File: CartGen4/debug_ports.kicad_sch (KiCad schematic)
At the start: 2 parts, among them J2 Conn_01x05_Male, J3 Conn_02x09_Odd_Even

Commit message: Switched from 1.00mm to 1.27mm pin headers
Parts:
- J2: footprint Connector_PinHeader_1.00mm:PinHeader_1x05_P1.00mm_Vertical -> Connector_PinHeader_1.27mm:PinHeader_1x05_P1.27mm_Vertical
- J3: footprint Connector_PinHeader_1.00mm:PinHeader_2x09_P1.00mm_Vertical -> Connector_PinHeader_1.27mm:PinHeader_2x09_P1.27mm_Vertical
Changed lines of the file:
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@@
     (property "Reference" "J2" (id 0) (at 69.215 85.09 0))
     (property "Value" "Conn_01x05_Male" (id 1) (at 69.215 87.63 0))
-    (property "Footprint" "Connector_PinHeader_1.00mm:PinHeader_1x05_P1.00mm_Vertical" (id 2) (at 68.58 95.25 0)
+    (property "Footprint" "Connector_PinHeader_1.27mm:PinHeader_1x05_P1.27mm_Vertical" (id 2) (at 68.58 95.25 0)
       (effects (font (size 1.27 1.27)) hide)
     )
@@
     (property "Reference" "J3" (id 0) (at 196.85 81.28 0))
     (property "Value" "Conn_02x09_Odd_Even" (id 1) (at 196.85 83.82 0))
-    (property "Footprint" "Connector_PinHeader_1.00mm:PinHeader_2x09_P1.00mm_Vertical" (id 2) (at 195.58 97.79 0)
+    (property "Footprint" "Connector_PinHeader_1.27mm:PinHeader_2x09_P1.27mm_Vertical" (id 2) (at 195.58 97.79 0)
       (effects (font (size 1.27 1.27)) hide)
     )

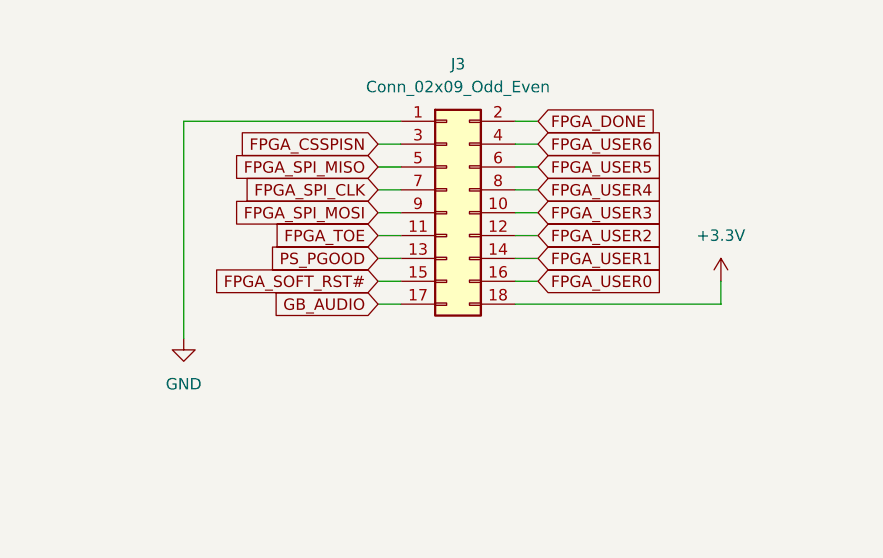
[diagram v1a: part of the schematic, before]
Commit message: Changed J3 to SMD header
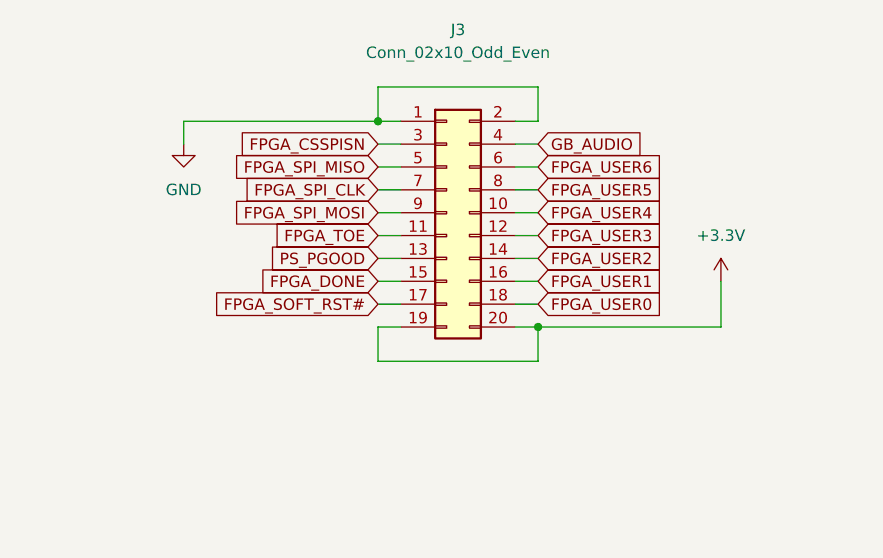
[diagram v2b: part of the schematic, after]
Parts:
- removed J3: Conn_02x09_Odd_Even, Connector_PinHeader_1.27mm:PinHeader_2x09_P1.27mm_Vertical, symbol Connector_Generic:Conn_02x09_Odd_Even
- added J3: Conn_02x10_Odd_Even, Connector:Conn_02x10, symbol Connector_Generic:Conn_02x10_Odd_Even
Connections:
- net +3V3: now also J3.19 (Pin_19), J3.20 (Pin_20)
- net FPGA_CSSPISN: now also J3.3 (Pin_3)
- net FPGA_DONE: now also J3.15 (Pin_15)
- net FPGA_SOFT_RST#: now also J3.17 (Pin_17)
- net FPGA_SPI_CLK: now also J3.7 (Pin_7)
- net FPGA_SPI_MISO: now also J3.5 (Pin_5)
- net FPGA_SPI_MOSI: now also J3.9 (Pin_9)
- net FPGA_TOE: now also J3.11 (Pin_11)
- net FPGA_USER0: now also J3.18 (Pin_18)
- net FPGA_USER1: now also J3.16 (Pin_16)
- net FPGA_USER2: now also J3.14 (Pin_14)
- net FPGA_USER3: now also J3.12 (Pin_12)
- net FPGA_USER4: now also J3.10 (Pin_10)
- net FPGA_USER5: now also J3.8 (Pin_8)
- net FPGA_USER6: now also J3.6 (Pin_6)
- net GB_AUDIO: now also J3.4 (Pin_4)
- net GND: now also J3.1 (Pin_1), J3.2 (Pin_2)
- net PS_PGOOD: now also J3.13 (Pin_13)

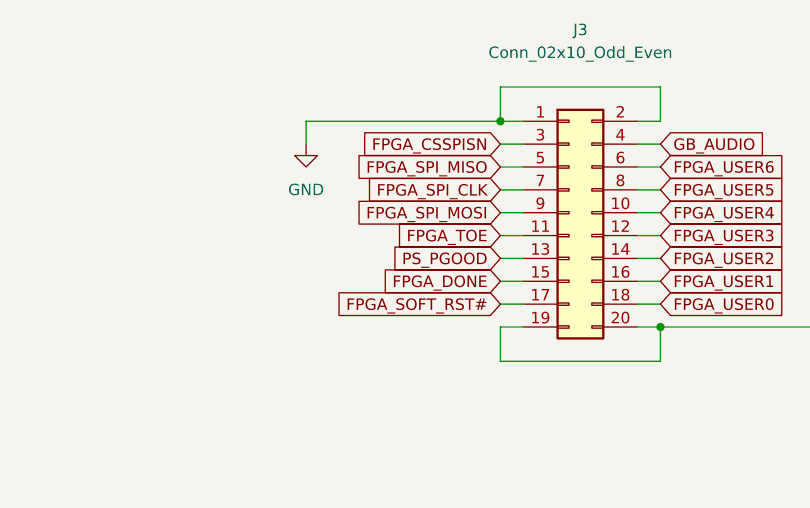
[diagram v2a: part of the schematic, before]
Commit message: Routed expansion port
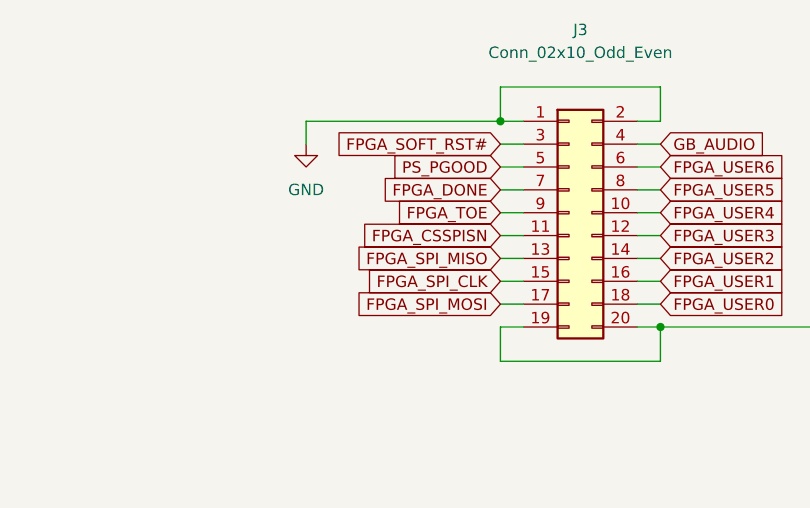
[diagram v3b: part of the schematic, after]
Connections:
- net FPGA_CSSPISN: now also J3.11 (Pin_11); no longer J3.3 (Pin_3)
- net FPGA_DONE: now also J3.7 (Pin_7); no longer J3.15 (Pin_15)
- net FPGA_SOFT_RST#: now also J3.3 (Pin_3); no longer J3.17 (Pin_17)
- net FPGA_SPI_CLK: now also J3.15 (Pin_15); no longer J3.7 (Pin_7)
- net FPGA_SPI_MISO: now also J3.13 (Pin_13); no longer J3.5 (Pin_5)
- net FPGA_SPI_MOSI: now also J3.17 (Pin_17); no longer J3.9 (Pin_9)
- net FPGA_TOE: now also J3.9 (Pin_9); no longer J3.11 (Pin_11)
- net PS_PGOOD: now also J3.5 (Pin_5); no longer J3.13 (Pin_13)

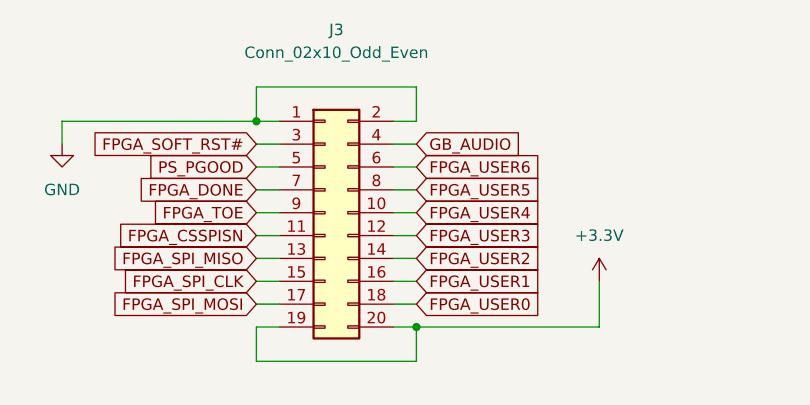
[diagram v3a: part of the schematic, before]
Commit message: Changed GB_AUDIO location for better noise isolation
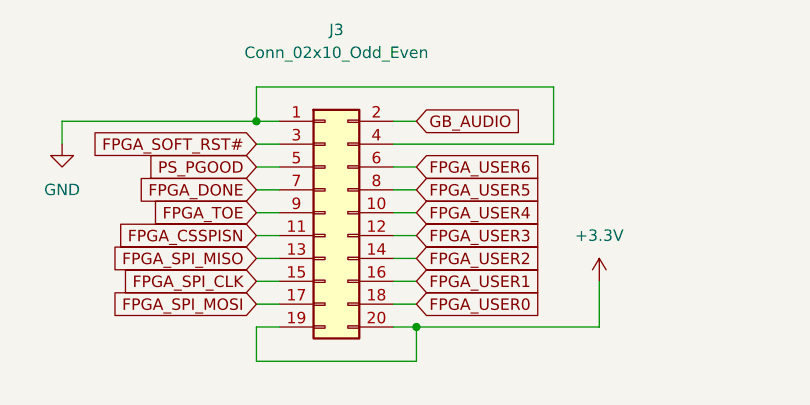
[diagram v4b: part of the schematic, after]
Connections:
- net GB_AUDIO: now also J3.2 (Pin_2); no longer J3.4 (Pin_4)
- net GND: now also J3.4 (Pin_4); no longer J3.2 (Pin_2)
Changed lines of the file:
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@@
     (stroke (width 0) (type default) (color 0 0 0 0))
   )
-  (wire (pts (xy 205.74 83.82) (xy 187.96 83.82))
+  (wire (pts (xy 187.96 83.82) (xy 220.98 83.82))
     (stroke (width 0) (type default) (color 0 0 0 0))
   )
@@
     (stroke (width 0) (type default) (color 0 0 0 0))
   )
+  (wire (pts (xy 203.2 87.63) (xy 205.74 87.63))
+    (stroke (width 0) (type default) (color 0 0 0 0))
+  )
+  (wire (pts (xy 220.98 90.17) (xy 203.2 90.17))
+    (stroke (width 0) (type default) (color 0 0 0 0))
+  )
   (wire (pts (xy 187.96 105.41) (xy 190.5 105.41))
     (stroke (width 0) (type default) (color 0 0 0 0))
   )
+  (wire (pts (xy 220.98 83.82) (xy 220.98 90.17))
+    (stroke (width 0) (type default) (color 0 0 0 0))
+  )
   (wire (pts (xy 73.66 97.79) (xy 76.2 97.79))
     (stroke (width 0) (type default) (color 0 0 0 0))
@@
     (stroke (width 0) (type default) (color 0 0 0 0))
   )
-  (wire (pts (xy 205.74 87.63) (xy 205.74 83.82))
-    (stroke (width 0) (type default) (color 0 0 0 0))
-  )
   (wire (pts (xy 187.96 87.63) (xy 166.37 87.63))
     (stroke (width 0) (type default) (color 0 0 0 0))
@@
     (stroke (width 0) (type default) (color 0 0 0 0))
   )
-  (wire (pts (xy 203.2 87.63) (xy 205.74 87.63))
-    (stroke (width 0) (type default) (color 0 0 0 0))
-  )
   (wire (pts (xy 166.37 87.63) (xy 166.37 90.17))
     (stroke (width 0) (type default) (color 0 0 0 0))
@@
   )
   (wire (pts (xy 73.66 90.17) (xy 97.79 90.17))
-    (stroke (width 0) (type default) (color 0 0 0 0))
-  )
-  (wire (pts (xy 203.2 90.17) (xy 205.74 90.17))
     (stroke (width 0) (type default) (color 0 0 0 0))
   )
@@
     )
   )
-  (global_label "GB_AUDIO" (shape input) (at 205.74 90.17 0) (fields_autoplaced)
-    (effects (font (size 1.27 1.27)) (justify left))
-    (property "Intersheet References" "${INTERSHEET_REFS}" (id 0) (at 217.285 90.2494 0)
-      (effects (font (size 1.27 1.27)) (justify left) hide)
-    )
+  (global_label "GB_AUDIO" (shape input) (at 205.74 87.63 0) (fields_autoplaced)
+    (effects (font (size 1.27 1.27)) (justify left))
+    (property "Intersheet References" "${INTERSHEET_REFS}" (id 0) (at 217.285 87.7094 0)
+      (effects (font (size 1.27 1.27)) (justify left) hide)
+    )

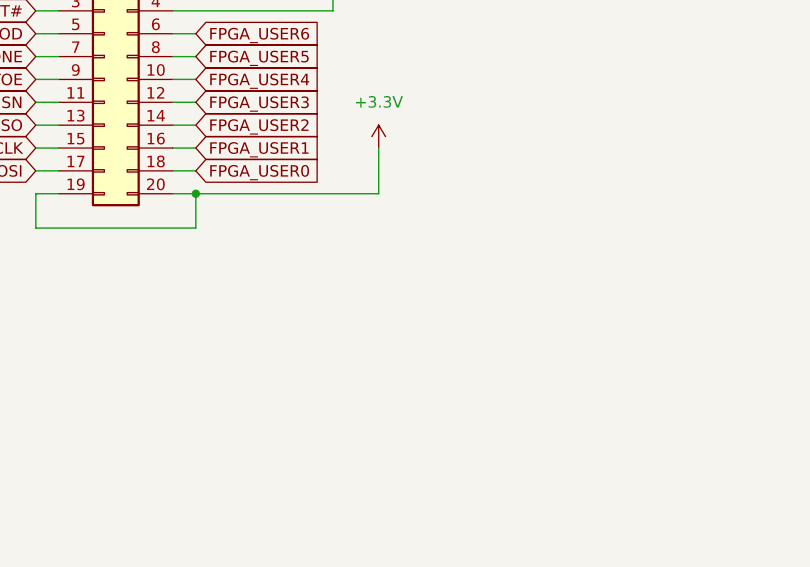
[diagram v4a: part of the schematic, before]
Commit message: Added decoupling cap to expansion header to be sure
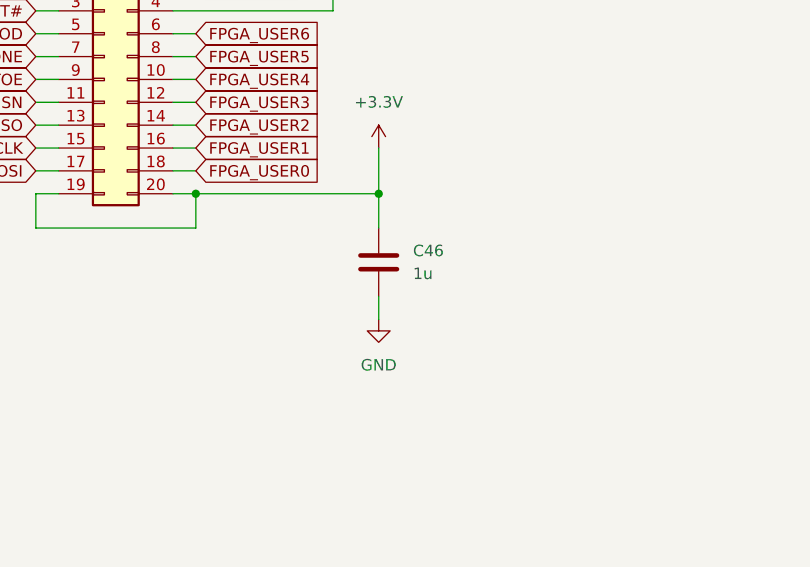
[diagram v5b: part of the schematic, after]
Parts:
- added C46: 1u, Capacitor_SMD:C_0603_1608Metric_Pad1.08x0.95mm_HandSolder, symbol Device:C
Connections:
- net +3V3: now also C46.1
- net GND: now also C46.2
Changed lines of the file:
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@@
     (company "© Elijah Almeida Coimbra")
   )
+  (junction (at 226.06 110.49) (diameter 0) (color 0 0 0 0)
+  )
   (junction (at 205.74 110.49) (diameter 0) (color 0 0 0 0)
   )
@@
     (stroke (width 0) (type default) (color 0 0 0 0))
   )
+  (wire (pts (xy 226.06 110.49) (xy 226.06 114.3))
+    (stroke (width 0) (type default) (color 0 0 0 0))
+  )
   (wire (pts (xy 187.96 97.79) (xy 190.5 97.79))
     (stroke (width 0) (type default) (color 0 0 0 0))
@@
   )
   (wire (pts (xy 203.2 97.79) (xy 205.74 97.79))
+    (stroke (width 0) (type default) (color 0 0 0 0))
+  )
+  (wire (pts (xy 226.06 121.92) (xy 226.06 124.46))
     (stroke (width 0) (type default) (color 0 0 0 0))
   )
@@
     (pin "1")
   )
+  (symbol (lib_id "Device:C") (at 226.06 118.11 0) (unit 1)
+    (in_bom yes) (on_board yes) (fields_autoplaced)
+    (property "Reference" "C46" (id 0) (at 229.87 116.8399 0)
+      (effects (font (size 1.27 1.27)) (justify left))
+    )
+    (property "Value" "1u" (id 1) (at 229.87 119.3799 0)
+      (effects (font (size 1.27 1.27)) (justify left))
+    )
+    (property "Footprint" "Capacitor_SMD:C_0603_1608Metric_Pad1.08x0.95mm_HandSolder" (id 2) (at 227.0252 121.92 0)
+      (effects (font (size 1.27 1.27)) hide)
+    )
+    (property "Datasheet" "~" (id 3) (at 226.06 118.11 0)
+      (effects (font (size 1.27 1.27)) hide)
+    )
+    (property "Critical" "N" (id 4) (at 226.06 118.11 0)
+      (effects (font (size 1.27 1.27)) hide)
+    )
+    (property "Notes" "Bypass capacitor for PWR/GND coupling." (id 5) (at 226.06 118.11 0)
+      (effects (font (size 1.27 1.27)) hide)
+    )
+    (property "Source" "ANY" (id 6) (at 226.06 118.11 0)
+      (effects (font (size 1.27 1.27)) hide)
+    )
+    (pin "1")
+    (pin "2")
+  )
   (symbol (lib_id "power:GND") (at 97.79 92.71 0) (unit 1)
     (in_bom yes) (on_board yes) (fields_autoplaced)
@@
       (effects (font (size 1.27 1.27)) hide)
     )
+    (pin "1")
+  )
+  (symbol (lib_id "power:GND") (at 226.06 124.46 0) (unit 1)
+    (in_bom yes) (on_board yes) (fields_autoplaced)
+    (property "Reference" "#PWR026" (id 0) (at 226.06 130.81 0)
+      (effects (font (size 1.27 1.27)) hide)
+    )
+    (property "Value" "GND" (id 1) (at 226.06 129.54 0))
+    (property "Footprint" "" (id 2) (at 226.06 124.46 0)
+      (effects (font (size 1.27 1.27)) hide)
+    )
+    (property "Datasheet" "" (id 3) (at 226.06 124.46 0)
+      (effects (font (size 1.27 1.27)) hide)
+    )

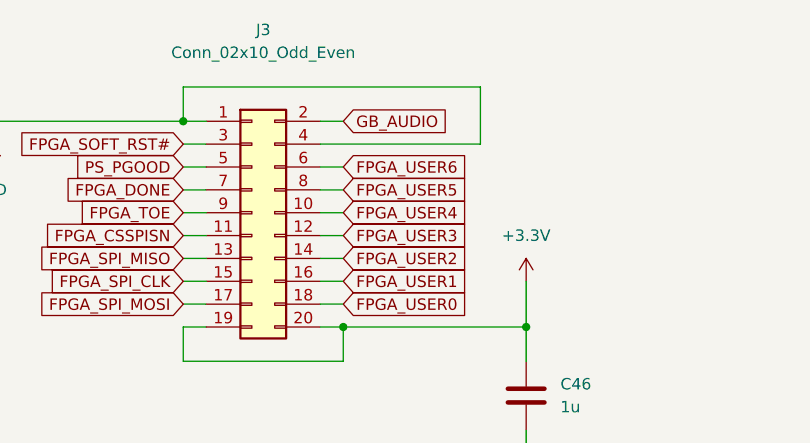
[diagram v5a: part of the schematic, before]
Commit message: Fixed GB_BUS_EN not being on 3V3 bank Added CLK_EN to ext clock
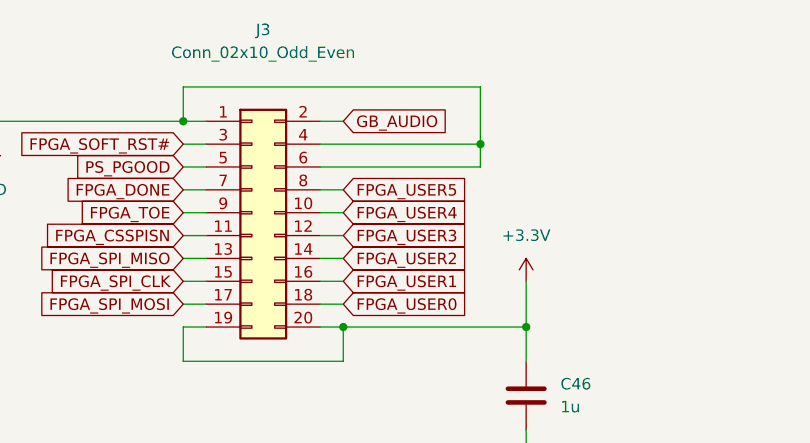
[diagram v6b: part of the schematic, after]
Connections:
- net FPGA_USER6 is gone; now on net GND: J3.6 (Pin_6)
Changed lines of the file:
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@@
   (junction (at 205.74 110.49) (diameter 0) (color 0 0 0 0)
+  )
+  (junction (at 220.98 90.17) (diameter 0) (color 0 0 0 0)
   )
   (junction (at 187.96 87.63) (diameter 0) (color 0 0 0 0)
@@
     (stroke (width 0) (type default) (color 0 0 0 0))
   )
-  (wire (pts (xy 203.2 92.71) (xy 205.74 92.71))
+  (wire (pts (xy 166.37 87.63) (xy 166.37 90.17))
     (stroke (width 0) (type default) (color 0 0 0 0))
   )
-  (wire (pts (xy 166.37 87.63) (xy 166.37 90.17))
+  (wire (pts (xy 203.2 92.71) (xy 220.98 92.71))
     (stroke (width 0) (type default) (color 0 0 0 0))
   )
@@
   )
   (wire (pts (xy 187.96 92.71) (xy 190.5 92.71))
+    (stroke (width 0) (type default) (color 0 0 0 0))
+  )
+  (wire (pts (xy 220.98 92.71) (xy 220.98 90.17))
     (stroke (width 0) (type default) (color 0 0 0 0))
   )
@@
     )
   )
-  (global_label "FPGA_USER6" (shape input) (at 205.74 92.71 0) (fields_autoplaced)
-    (effects (font (size 1.27 1.27)) (justify left))
-    (property "Intersheet References" "${INTERSHEET_REFS}" (id 0) (at 220.0064 92.7894 0)
-      (effects (font (size 1.27 1.27)) (justify left) hide)
-    )
-  )

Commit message: Updated field information
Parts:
- C46: Package ID (none) -> 0603
- J2: Critical (none) -> N; Source (none) -> ANY
- J3: Critical (none) -> N; Source (none) -> SPEC
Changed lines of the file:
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@@
       (effects (font (size 1.27 1.27)) hide)
     )
-    (property "Datasheet" "~" (id 3) (at 195.58 97.79 0)
+    (property "Datasheet" "https://nl.aliexpress.com/item/4000280789459.html?spm=a2g0o.order_list.order_list_main.10.7b0279d22xo7Wf&gatewayAdapt=glo2nld" (id 3) (at 195.58 97.79 0)
+      (effects (font (size 1.27 1.27)) hide)
+    )
+    (property "Critical" "N" (id 4) (at 195.58 97.79 0)
+      (effects (font (size 1.27 1.27)) hide)
+    )
+    (property "Notes" "~" (id 5) (at 195.58 97.79 0)
+      (effects (font (size 1.27 1.27)) hide)
+    )
+    (property "Description" "Debug/expansion port" (id 6) (at 195.58 97.79 0)
+      (effects (font (size 1.27 1.27)) hide)
+    )
+    (property "Package ID" "~" (id 7) (at 195.58 97.79 0)
+      (effects (font (size 1.27 1.27)) hide)
+    )
+    (property "Source" "SPEC" (id 8) (at 195.58 97.79 0)
+      (effects (font (size 1.27 1.27)) hide)
+    )
+    (property "MFN" "~" (id 9) (at 195.58 97.79 0)
+      (effects (font (size 1.27 1.27)) hide)
+    )
+    (property "MFP" "~" (id 10) (at 195.58 97.79 0)
       (effects (font (size 1.27 1.27)) hide)
     )
@@
       (effects (font (size 1.27 1.27)) hide)
     )
+    (property "Description" "~" (id 7) (at 226.06 118.11 0)
+      (effects (font (size 1.27 1.27)) hide)
+    )
+    (property "MFN" "~" (id 8) (at 226.06 118.11 0)
+      (effects (font (size 1.27 1.27)) hide)
+    )
+    (property "MFP" "~" (id 9) (at 226.06 118.11 0)
+      (effects (font (size 1.27 1.27)) hide)
+    )
+    (property "Package ID" "0603" (id 10) (at 226.06 118.11 0)
+      (effects (font (size 1.27 1.27)) hide)
+    )
     (pin "1")
     (pin "2")
@@
       (effects (font (size 1.27 1.27)) hide)
     )
+    (property "Critical" "N" (id 4) (at 68.58 95.25 0)
+      (effects (font (size 1.27 1.27)) hide)
+    )
+    (property "Notes" "~" (id 5) (at 68.58 95.25 0)
+      (effects (font (size 1.27 1.27)) hide)
+    )
+    (property "Description" "JTAG header" (id 6) (at 68.58 95.25 0)
+      (effects (font (size 1.27 1.27)) hide)
+    )
+    (property "Package ID" "~" (id 7) (at 68.58 95.25 0)
+      (effects (font (size 1.27 1.27)) hide)
+    )
+    (property "Source" "ANY" (id 8) (at 68.58 95.25 0)
+      (effects (font (size 1.27 1.27)) hide)
+    )
+    (property "MFN" "~" (id 9) (at 68.58 95.25 0)
+      (effects (font (size 1.27 1.27)) hide)
+    )
+    (property "MFP" "~" (id 10) (at 68.58 95.25 0)
+      (effects (font (size 1.27 1.27)) hide)
+    )
